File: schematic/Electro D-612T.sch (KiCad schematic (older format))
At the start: 8 parts

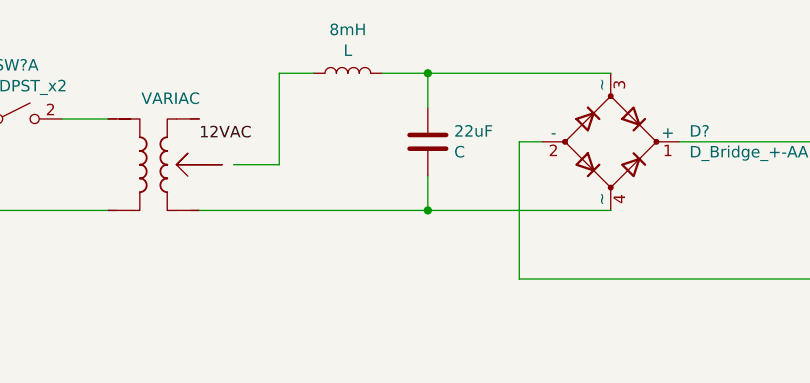
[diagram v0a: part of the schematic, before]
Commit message: Fixed capacitor orientation in circuit.
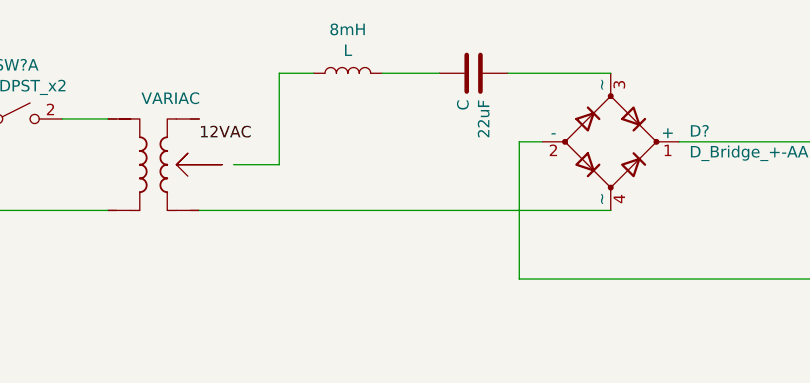
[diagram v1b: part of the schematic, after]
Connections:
- wire segments 25 -> 22
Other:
- moved on the sheet: 22uF
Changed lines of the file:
@@
 	5150 3200 5300 3200
-Wire Wire Line
-	5600 3200 5800 3200
-Wire Wire Line
-	4800 3800 5800 3800
-Wire Wire Line
-	5800 3350 5800 3200
-Connection ~ 5800 3200
-Wire Wire Line
-	5800 3650 5800 3800
-Connection ~ 5800 3800
-Wire Wire Line
-	5800 3200 6600 3200
-Wire Wire Line
-	5800 3800 6600 3800
 Wire Wire Line
 	6200 4100 8700 4100
@@
 L Device:C 22uF
 U 1 1 5F991895
-P 5800 3500
-F 0 "22uF" H 5915 3546 50  0000 L CNN
-F 1 "C" H 5915 3455 50  0000 L CNN
-F 2 "" H 5838 3350 50  0001 C CNN
-F 3 "~" H 5800 3500 50  0001 C CNN
-	1    5800 3500
-	1    0    0    -1
+P 6000 3200
+F 0 "22uF" H 6115 3246 50  0000 L CNN
+F 1 "C" H 6115 3155 50  0000 L CNN
+F 2 "" H 6038 3050 50  0001 C CNN
+F 3 "~" H 6000 3200 50  0001 C CNN
+	1    6000 3200
+	0    1    1    0
 $EndComp
 Text Label 4800 3500 0    50   ~ 0
@@
 Wire Wire Line
 	4950 3600 5150 3600
+Wire Wire Line
+	4800 3800 6600 3800
+Wire Wire Line
+	5600 3200 5850 3200
+Wire Wire Line
+	6150 3200 6600 3200
 $EndSCHEMATC

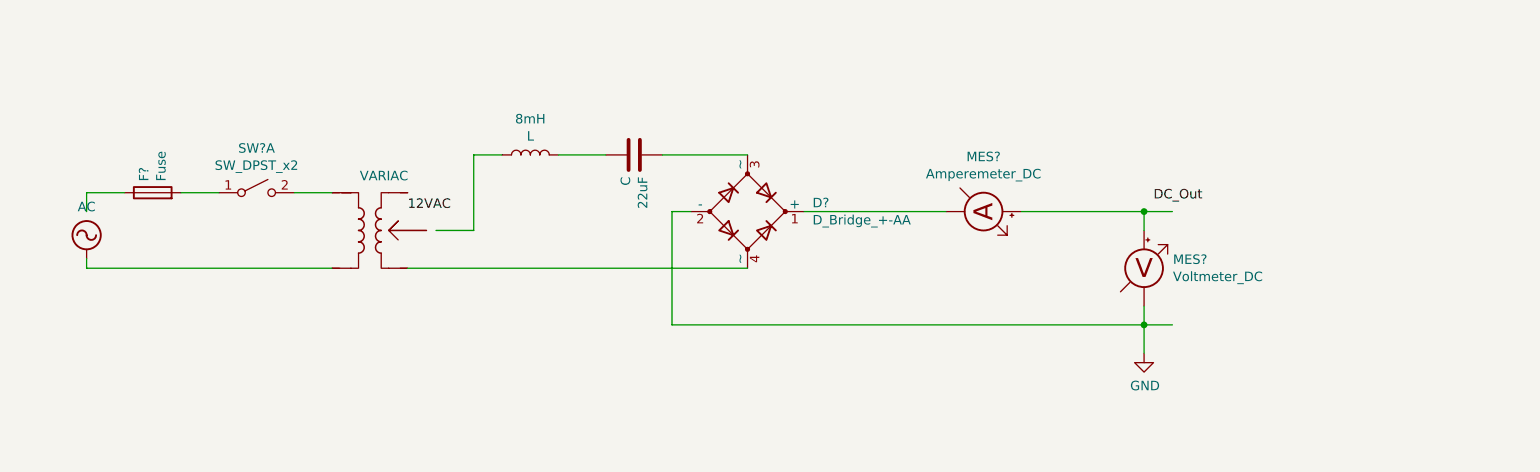
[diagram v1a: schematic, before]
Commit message: Updated schematic with addition of neon lamp, and capacitor discharge circuit.
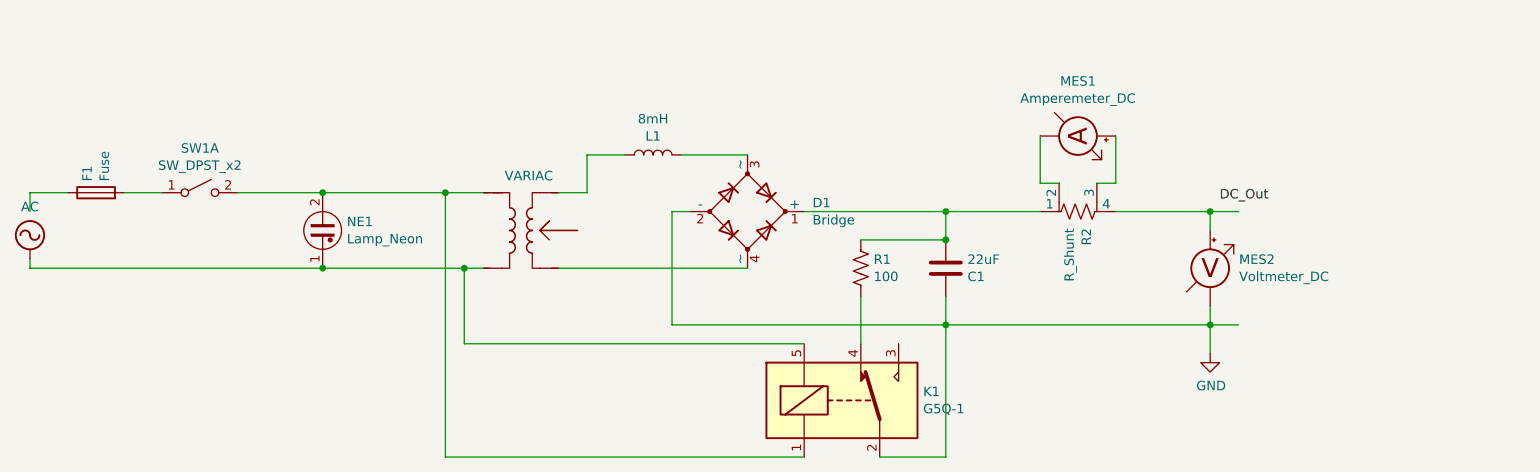
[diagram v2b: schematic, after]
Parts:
- removed VAR?: VARIAC, symbol Transformer:VARIAC
- added K1: G5Q-1, Relay_THT:Relay_SPDT_Omron-G5Q-1, symbol Relay:G5Q-1
- added NE1: Lamp_Neon, symbol Device:Lamp_Neon
- added R1: 100, symbol Device:R_US
- added R2: R_Shunt, symbol Device:R_Shunt_US
- added VR?: VARIAC, symbol Transformer:VARIAC
- 22uF: value C -> C1
- 8mH: value L -> L1
- D1: renamed from D?; value D_Bridge_+-AA -> Bridge
- gave numbers to parts that had none: 4
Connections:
- net labels removed: 12VAC
- wire segments 22 -> 41
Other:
- moved on the sheet: 22uF, 8mH, F1, MES1, MES2, SW1A

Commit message: Removed relay discharge circuit.
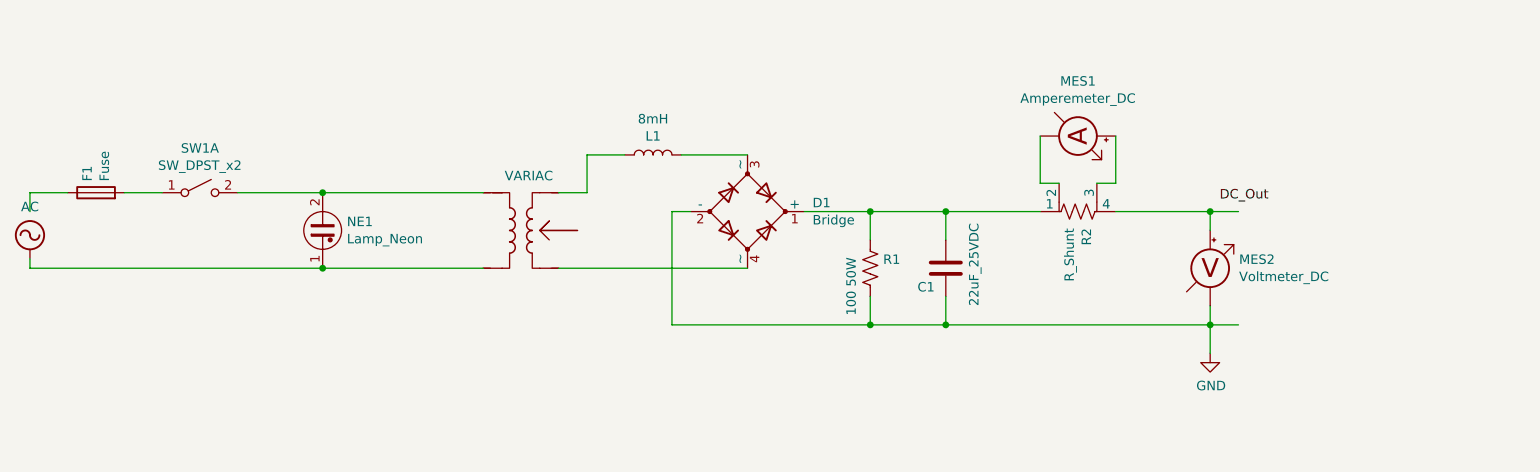
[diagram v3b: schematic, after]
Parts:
- removed K1: G5Q-1, Relay_THT:Relay_SPDT_Omron-G5Q-1, symbol Relay:G5Q-1
- R1: value 100 -> 100 50W
- renumbered 22uF to 22uF_25VDC
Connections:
- wire segments 41 -> 35
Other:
- moved on the sheet: R1
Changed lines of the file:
@@
 	6200 3500 6200 4100
 Wire Wire Line
-	6200 4100 7650 4100
+	6200 4100 7250 4100
 $Comp
 L Device:D_Bridge_+-AA D1
@@
 $EndComp
 Wire Wire Line
-	6900 3500 7650 3500
+	6900 3500 7250 3500
 $Comp
-L Device:C 22uF
+L Device:C 22uF_25VDC
 U 1 1 5F991895
 P 7650 3800
-F 0 "22uF" H 7765 3846 50  0000 L CNN
-F 1 "C1" H 7765 3755 50  0000 L CNN
+F 0 "22uF_25VDC" V 7800 3600 50  0000 L CNN
+F 1 "C1" H 7500 3700 50  0000 L CNN
 F 2 "" H 7688 3650 50  0001 C CNN
 F 3 "~" H 7650 3800 50  0001 C CNN
@@
 $EndComp
 $Comp
-L Relay:G5Q-1 K1
-U 1 1 5FBB4F94
-P 7100 4500
-F 0 "K1" H 7530 4546 50  0000 L CNN
-F 1 "G5Q-1" H 7530 4455 50  0000 L CNN
-F 2 "Relay_THT:Relay_SPDT_Omron-G5Q-1" H 7550 4450 50  0001 L CNN
-F 3 "https://www.omron.com/ecb/products/pdf/en-g5q.pdf" H 7100 4500 50  0001 L CNN
-	1    7100 4500
-	1    0    0    -1
-$EndComp
-$Comp
 L Device:R_US R1
 U 1 1 5FBC3736
-P 7200 3800
-F 0 "R1" H 7268 3846 50  0000 L CNN
-F 1 "100" H 7268 3755 50  0000 L CNN
-F 2 "" V 7240 3790 50  0001 C CNN
-F 3 "~" H 7200 3800 50  0001 C CNN
-	1    7200 3800
+P 7250 3800
+F 0 "R1" H 7318 3846 50  0000 L CNN
+F 1 " 100 50W" V 7150 3550 50  0000 L CNN
+F 2 "" V 7290 3790 50  0001 C CNN
+F 3 "~" H 7250 3800 50  0001 C CNN
+	1    7250 3800
 	1    0    0    -1
 $EndComp
@@
 Wire Wire Line
 	2800 3800 4350 3800
-Wire Wire Line
-	7200 3650 7650 3650
-Connection ~ 7650 3650
-Wire Wire Line
-	7200 3950 7200 4200
-Wire Wire Line
-	7300 4800 7650 4800
-Wire Wire Line
-	7650 4800 7650 4100
-Wire Wire Line
-	5100 3800 5100 4200
-Wire Wire Line
-	5100 4200 6900 4200
 $Comp
 L Transformer:VARIAC VR?
@@
 Wire Wire Line
 	8150 3350 8150 3100
+Connection ~ 4350 3400
+Connection ~ 4350 3800
 Wire Wire Line
-	4350 3400 5000 3400
-Connection ~ 4350 3400
+	4350 3800 5200 3800
 Wire Wire Line
-	4350 3800 5100 3800
-Connection ~ 4350 3800
-Connection ~ 5100 3800
+	4350 3400 5200 3400
 Wire Wire Line
-	5100 3800 5200 3800
+	7250 3650 7250 3500
+Connection ~ 7250 3500
 Wire Wire Line
-	6900 4800 5000 4800
+	7250 3500 7650 3500
 Wire Wire Line
-	5000 4800 5000 3400
-Connection ~ 5000 3400
+	7250 3950 7250 4100
+Connection ~ 7250 4100
 Wire Wire Line
-	5000 3400 5200 3400
+	7250 4100 7650 4100
 $EndSCHEMATC

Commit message: Fixed choke location, and updated discharge resistor value.
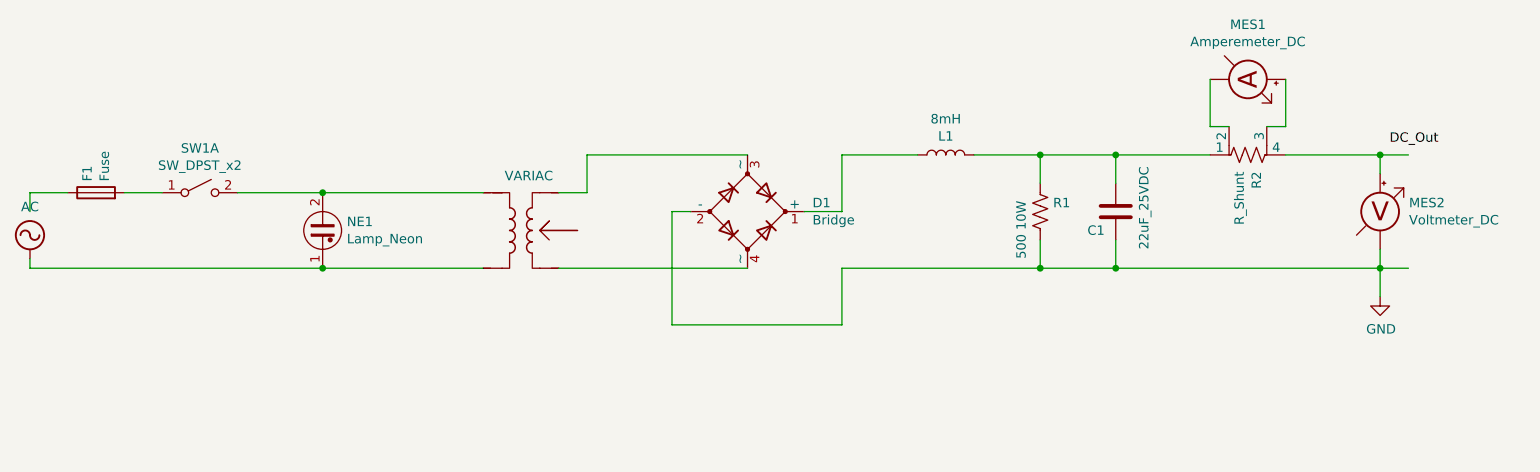
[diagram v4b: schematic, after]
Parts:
- R1: value 100 50W -> 500 10W
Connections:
- wire segments 35 -> 39
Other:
- moved on the sheet: 22uF_25VDC, 8mH, MES1, MES2, R1, R2
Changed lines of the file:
@@
 $EndComp
 Wire Wire Line
-	9050 3500 9050 3600
-Wire Wire Line
-	9050 4000 9050 4100
+	9950 3200 9950 3300
+Wire Wire Line
+	9950 3700 9950 3800
 $Comp
 L Device:Amperemeter_DC MES1
 U 1 1 5F7AC952
-P 8350 3100
-F 0 "MES1" V 8060 3100 50  0000 C CNN
-F 1 "Amperemeter_DC" V 8151 3100 50  0000 C CNN
-F 2 "" V 8350 3200 50  0001 C CNN
-F 3 "~" V 8350 3200 50  0001 C CNN
-	1    8350 3100
+P 9250 2800
+F 0 "MES1" V 8960 2800 50  0000 C CNN
+F 1 "Amperemeter_DC" V 9051 2800 50  0000 C CNN
+F 2 "" V 9250 2900 50  0001 C CNN
+F 3 "~" V 9250 2900 50  0001 C CNN
+	1    9250 2800
 	0    1    1    0
 $EndComp
@@
 L Device:Voltmeter_DC MES2
 U 1 1 5F7AB8A0
-P 9050 3800
-F 0 "MES2" H 9203 3846 50  0000 L CNN
-F 1 "Voltmeter_DC" H 9203 3755 50  0000 L CNN
-F 2 "" V 9050 3900 50  0001 C CNN
-F 3 "~" V 9050 3900 50  0001 C CNN
-	1    9050 3800
-	1    0    0    -1
-$EndComp
-Wire Wire Line
-	9200 3500 9050 3500
-Wire Wire Line
-	9200 4100 9050 4100
-Connection ~ 9050 4100
+P 9950 3500
+F 0 "MES2" H 10103 3546 50  0000 L CNN
+F 1 "Voltmeter_DC" H 10103 3455 50  0000 L CNN
+F 2 "" V 9950 3600 50  0001 C CNN
+F 3 "~" V 9950 3600 50  0001 C CNN
+	1    9950 3500
+	1    0    0    -1
+$EndComp
+Wire Wire Line
+	10100 3200 9950 3200
+Wire Wire Line
+	10100 3800 9950 3800
+Connection ~ 9950 3800
 Wire Wire Line
 	2800 3500 2800 3400
 Wire Wire Line
 	2800 3750 2800 3800
-Text Label 9100 3450 0    50   ~ 0
+Text Label 10000 3150 0    50   ~ 0
 DC_Out
 $Comp
@@
 L power:GND #PWR?
 U 1 1 5F993FA2
-P 9050 4250
-F 0 "#PWR?" H 9050 4000 50  0001 C CNN
-F 1 "GND" H 9055 4077 50  0000 C CNN
-F 2 "" H 9050 4250 50  0001 C CNN
-F 3 "" H 9050 4250 50  0001 C CNN
-	1    9050 4250
-	1    0    0    -1
-$EndComp
-Wire Wire Line
-	9050 4100 9050 4250
+P 9950 3950
+F 0 "#PWR?" H 9950 3700 50  0001 C CNN
+F 1 "GND" H 9955 3777 50  0000 C CNN
+F 2 "" H 9950 3950 50  0001 C CNN
+F 3 "" H 9950 3950 50  0001 C CNN
+	1    9950 3950
+	1    0    0    -1
+$EndComp
+Wire Wire Line
+	9950 3800 9950 3950
 Wire Wire Line
 	6300 3500 6200 3500
@@
 L Device:L 8mH
 U 1 1 5F9693F8
-P 6100 3200
-F 0 "8mH" V 6290 3200 50  0000 C CNN
-F 1 "L1" V 6199 3200 50  0000 C CNN
-F 2 "" H 6100 3200 50  0001 C CNN
-F 3 "~" H 6100 3200 50  0001 C CNN
-	1    6100 3200
+P 7650 3200
+F 0 "8mH" V 7840 3200 50  0000 C CNN
+F 1 "L1" V 7749 3200 50  0000 C CNN
+F 2 "" H 7650 3200 50  0001 C CNN
+F 3 "~" H 7650 3200 50  0001 C CNN
+	1    7650 3200
 	0    -1   -1   0
 $EndComp
@@
 	6200 3500 6200 4100
 Wire Wire Line
-	6200 4100 7250 4100
+	7100 3800 8150 3800
 $Comp
 L Device:D_Bridge_+-AA D1
@@
 $EndComp
 Wire Wire Line
-	6900 3500 7250 3500
+	7800 3200 8150 3200
 $Comp
 L Device:C 22uF_25VDC
 U 1 1 5F991895
-P 7650 3800
-F 0 "22uF_25VDC" V 7800 3600 50  0000 L CNN
-F 1 "C1" H 7500 3700 50  0000 L CNN
-F 2 "" H 7688 3650 50  0001 C CNN
-F 3 "~" H 7650 3800 50  0001 C CNN
-	1    7650 3800
-	1    0    0    -1
-$EndComp
-Wire Wire Line
-	7650 3500 7650 3650
-Wire Wire Line
-	7650 3950 7650 4100
-Connection ~ 7650 4100
+P 8550 3500
+F 0 "22uF_25VDC" V 8700 3300 50  0000 L CNN
+F 1 "C1" H 8400 3400 50  0000 L CNN
+F 2 "" H 8588 3350 50  0001 C CNN
+F 3 "~" H 8550 3500 50  0001 C CNN
+	1    8550 3500
+	1    0    0    -1
+$EndComp
+Wire Wire Line
+	8550 3200 8550 3350
+Wire Wire Line
+	8550 3650 8550 3800
+Connection ~ 8550 3800
 Wire Wire Line
 	5600 3800 6600 3800
-Wire Wire Line
-	5750 3200 5950 3200
-Wire Wire Line
-	6250 3200 6600 3200
 $Comp
 L Device:Lamp_Neon NE1
@@
 L Device:R_US R1
 U 1 1 5FBC3736
-P 7250 3800
-F 0 "R1" H 7318 3846 50  0000 L CNN
-F 1 " 100 50W" V 7150 3550 50  0000 L CNN
-F 2 "" V 7290 3790 50  0001 C CNN
-F 3 "~" H 7250 3800 50  0001 C CNN
-	1    7250 3800
+P 8150 3500
+F 0 "R1" H 8218 3546 50  0000 L CNN
+F 1 " 500 10W" V 8050 3250 50  0000 L CNN
+F 2 "" V 8190 3490 50  0001 C CNN
+F 3 "~" H 8150 3500 50  0001 C CNN
+	1    8150 3500
 	1    0    0    -1
 $EndComp
@@
 	5750 3400 5600 3400
 Wire Wire Line
-	7650 4100 9050 4100
+	8550 3800 9950 3800
 $Comp
 L Device:R_Shunt_US R2
 U 1 1 5FBE8B50
-P 8350 3500
-F 0 "R2" H 8262 3454 50  0000 R CNN
-F 1 "R_Shunt" H 8262 3545 50  0000 R CNN
-F 2 "" V 8280 3500 50  0001 C CNN
-F 3 "~" H 8350 3500 50  0001 C CNN
-	1    8350 3500
+P 9250 3200
+F 0 "R2" H 9162 3154 50  0000 R CNN
+F 1 "R_Shunt" H 9162 3245 50  0000 R CNN
+F 2 "" V 9180 3200 50  0001 C CNN
+F 3 "~" H 9250 3200 50  0001 C CNN
+	1    9250 3200
 	0    -1   -1   0
 $EndComp
 Wire Wire Line
-	9050 3500 8550 3500
-Connection ~ 9050 3500
-Wire Wire Line
-	7650 3500 8150 3500
-Connection ~ 7650 3500
-Wire Wire Line
-	8550 3100 8550 3350
-Wire Wire Line
-	8550 3350 8450 3350
-Wire Wire Line
-	8250 3350 8150 3350
-Wire Wire Line
-	8150 3350 8150 3100
+	9950 3200 9450 3200
+Connection ~ 9950 3200
+Wire Wire Line
+	8550 3200 9050 3200
+Connection ~ 8550 3200
+Wire Wire Line
+	9450 2800 9450 3050
+Wire Wire Line
+	9450 3050 9350 3050
+Wire Wire Line
+	9150 3050 9050 3050
+Wire Wire Line
+	9050 3050 9050 2800
 Connection ~ 4350 3400
 Connection ~ 4350 3800
@@
 	4350 3400 5200 3400
 Wire Wire Line
-	7250 3650 7250 3500
-Connection ~ 7250 3500
-Wire Wire Line
-	7250 3500 7650 3500
-Wire Wire Line
-	7250 3950 7250 4100
-Connection ~ 7250 4100
-Wire Wire Line
-	7250 4100 7650 4100
+	8150 3350 8150 3200
+Connection ~ 8150 3200
+Wire Wire Line
+	8150 3200 8550 3200
+Wire Wire Line
+	8150 3650 8150 3800
+Connection ~ 8150 3800
+Wire Wire Line
+	8150 3800 8550 3800
+Wire Wire Line
+	5750 3200 6600 3200
+Wire Wire Line
+	7100 3500 7100 3200
+Wire Wire Line
+	7100 3200 7500 3200
+Wire Wire Line
+	6900 3500 7100 3500
+Wire Wire Line
+	7100 3800 7100 4100
+Wire Wire Line
+	7100 4100 6200 4100
 $EndSCHEMATC
